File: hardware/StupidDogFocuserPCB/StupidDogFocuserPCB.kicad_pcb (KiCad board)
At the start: 2 copper layers, 68.6 x 53.3 mm, 18 parts, among them M1 Stepper_Motor_bipolar, SW1 Rotary_Encoder_Switch, U1 DHT11, U2 SN74HC14N

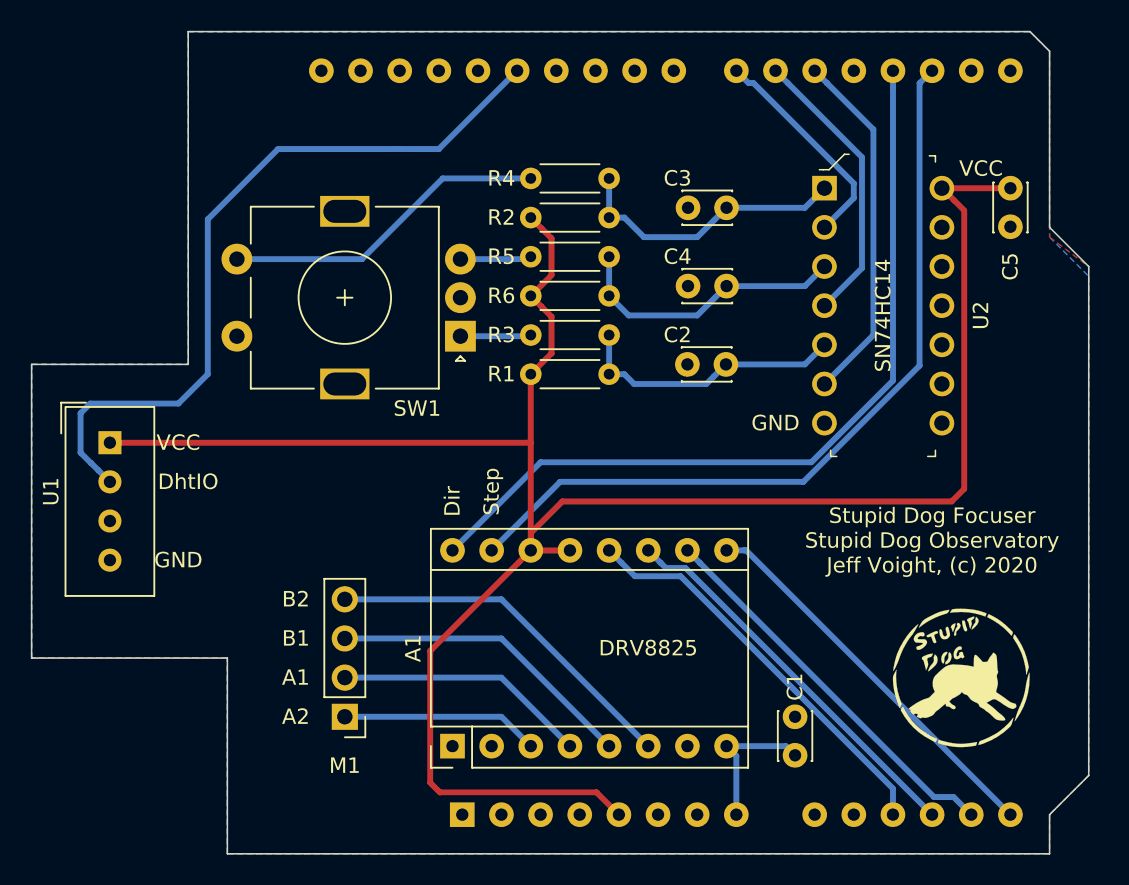
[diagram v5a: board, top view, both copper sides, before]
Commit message: Updated schematic. Added limit switch. Moved encoder to the right and the stepper to the left. Adjusted resistor and capacitor sizes. Added screw terminals. Moved DHT11 to where it can bend out.
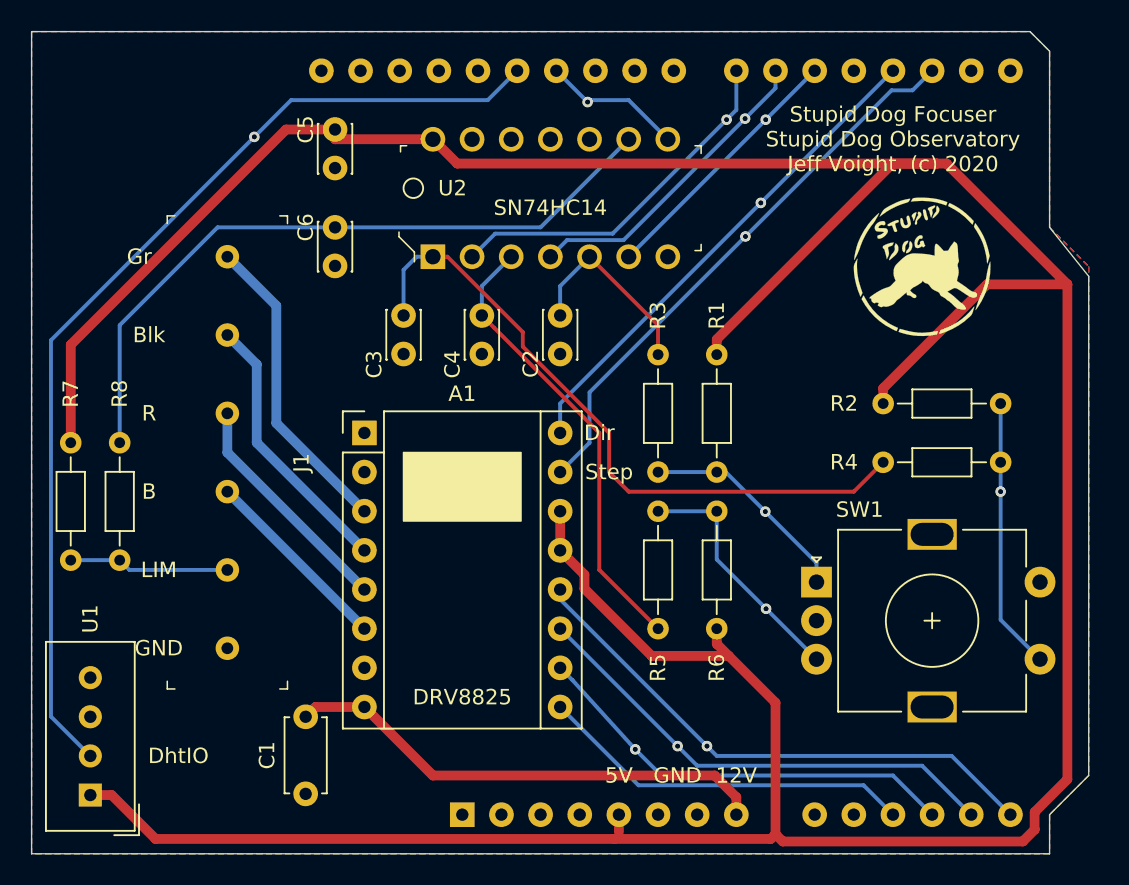
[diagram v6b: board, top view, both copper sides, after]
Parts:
- removed M1: Stepper_Motor_bipolar, Connector_PinHeader_2.54mm:PinHeader_1x04_P2.54mm_Vertical
- added C6: 4.7uF, Capacitor_THT:C_Disc_D3.0mm_W2.0mm_P2.50mm, F.Cu at (114.9, 69.8)
- added J1: OSTTC062162, digikey-footprints:Term_Block_1x6_P5.08mm, F.Cu at (108.0, 71.8)
- added R7: 1k, Resistor_THT:R_Axial_DIN0204_L3.6mm_D1.6mm_P7.62mm_Horizontal, F.Cu at (97.8, 83.8)
- added R8: 1k, Resistor_THT:R_Axial_DIN0204_L3.6mm_D1.6mm_P7.62mm_Horizontal, F.Cu at (101.0, 83.8)
- C1: footprint Capacitor_THT:C_Disc_D3.0mm_W2.0mm_P2.50mm -> Capacitor_THT:C_Disc_D4.7mm_W2.5mm_P5.00mm
- R1, R2, R3, R4, R5, R6: footprint Resistor_THT:R_Axial_DIN0204_L3.6mm_D1.6mm_P5.08mm_Horizontal -> Resistor_THT:R_Axial_DIN0204_L3.6mm_D1.6mm_P7.62mm_Horizontal
- moved C5 44.0 mm to (114.9, 63.5)
- moved C1 32.1 mm to (113.0, 106.6), turned to 90 degrees
- moved SW1 28.1 mm to (146.2, 92.9), turned to 0 degrees
- moved G1 26.8 mm to (153.0, 72.4)
- moved R2 25.8 mm to (150.5, 81.3)
- moved U2 25.8 mm to (121.3, 71.8), turned to 90 degrees
- moved R4 25.6 mm to (150.5, 85.1), turned to 0 degrees
- moved U1 22.9 mm to (99.1, 106.7), turned to 180 degrees
- moved C3 22.1 mm to (119.4, 75.6), turned to 270 degrees
- moved A1 21.1 mm to (116.8, 83.2), turned to 0 degrees
- moved R5 18.5 mm to (135.9, 88.3), turned to 270 degrees
- moved R6 15.6 mm to (139.7, 88.3), turned to 270 degrees
- moved C4 14.1 mm to (124.5, 78.1), turned to 90 degrees
- moved R1 12.1 mm to (139.7, 78.1), turned to 270 degrees
- moved C2 11.2 mm to (129.5, 75.6), turned to 270 degrees
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- renumbered G*** to G1
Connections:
- A1 pad 3: A2 -> G
- A1 pad 4: A1 -> BLK
- A1 pad 5: B1 -> R
- A1 pad 6: B2 -> BL
- A2 pad 11: M2 -> ~Enable
- A2 pad 12: M1 -> M0
- A2 pad 13: M0 -> M1
- A2 pad 14: ~Enable -> M2
- A2 pad 20: ENCA_A -> ENCA
- A2 pad 21: ENCB_A -> ENCB
- A2 pad 22: SW_A -> SW
- A2 pad 26: (no net) -> LIM
- C2 pad 1: ENC_A -> ENCA_A
- C3 pad 1: SW -> SW_A
- C4 pad 2: ENC_B -> ENCB_A
- R1 pad 2: ENC_A -> Net-(R1-Pad2)
- R2 pad 2: SW -> Net-(R2-Pad2)
- R3 pad 1: ENC_A -> ENCA_A
- R3 pad 2: Net-(R3-Pad2) -> Net-(R1-Pad2)
- R4 pad 1: SW -> SW_A
- R4 pad 2: Net-(R4-Pad2) -> Net-(R2-Pad2)
- R5 pad 2: ENC_B -> ENCB_A
- R6 pad 1: ENC_B -> Net-(R5-Pad1)
- SW1 pad A: Net-(R3-Pad2) -> Net-(R1-Pad2)
- SW1 pad S1: Net-(R4-Pad2) -> Net-(R2-Pad2)
- U2 pad 1: SW -> SW_A
- U2 pad 2: SW_A -> SW
- U2 pad 3: ENC_B -> ENCB_A
- U2 pad 4: ENCB_A -> ENCB
- U2 pad 5: ENC_A -> ENCA_A
- U2 pad 6: ENCA_A -> ENCA
- U2 pad 8: (no net) -> LIM
- U2 pad 9: (no net) -> LIM_A
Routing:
- net VCC: track 139.5 -> 251.0 mm
- net LIM_A: track 0.00 -> 45.6 mm
- net SW_A: track 14.3 -> 43.6 mm
- net B2: track 23.6 -> 0.00 mm
- net VDD: track 9.40 -> 31.8 mm
- net Net-(R4-Pad2): track 21.2 -> 0.00 mm
- net Dir: track 53.2 -> 32.4 mm, vias 0 -> 1
- net ENCB: track 0.00 -> 20.3 mm, vias 0 -> 1
- net G: track 0.00 -> 20.2 mm
- net B1: track 20.0 -> 0.00 mm
- net ENC_B: track 18.4 -> 0.00 mm
- net ENC_A: track 17.8 -> 0.00 mm
- net BLK: track 0.00 -> 17.7 mm
- net Net-(R2-Pad2): track 0.00 -> 17.6 mm, vias 0 -> 1
- net ENCA: track 0.00 -> 17.1 mm, vias 0 -> 1
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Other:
- outline, holes or cut-outs redrawn
- board text added: "12V"
- board text added: "5V"
- board text added: "B"
- board text added: "Blk"
- board text added: "Gr"
- board text added: "LIM"
- board text added: "R"
- board text removed: "A1"
- board text removed: "A2"
- board text removed: "B1"
- board text removed: "B2"
- board text removed: "VCC"

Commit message: thicker traces for the home gamer. Cleanup bends. Moved test points around.
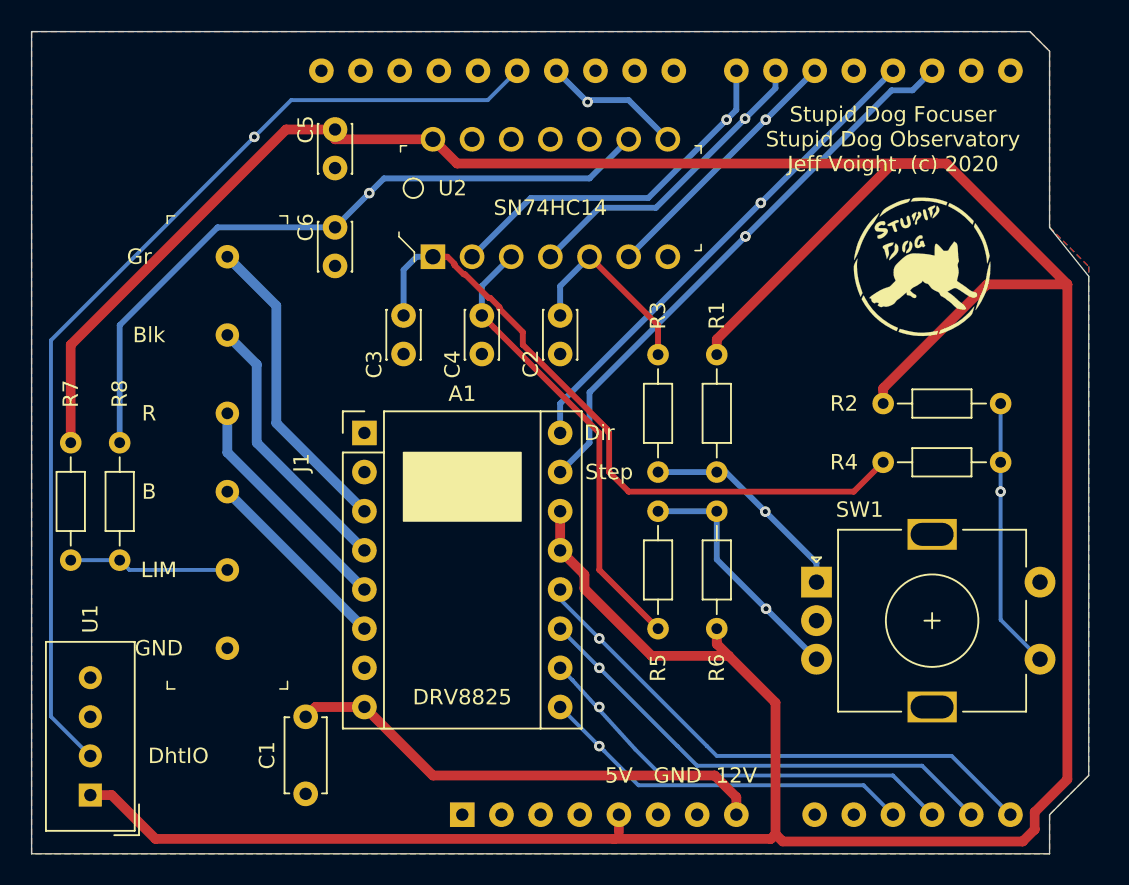
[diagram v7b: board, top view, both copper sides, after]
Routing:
- net LIM_A: vias 0 -> 1
- net ~Enable: vias 0 -> 1
